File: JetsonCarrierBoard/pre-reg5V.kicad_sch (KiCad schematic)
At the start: 18 parts

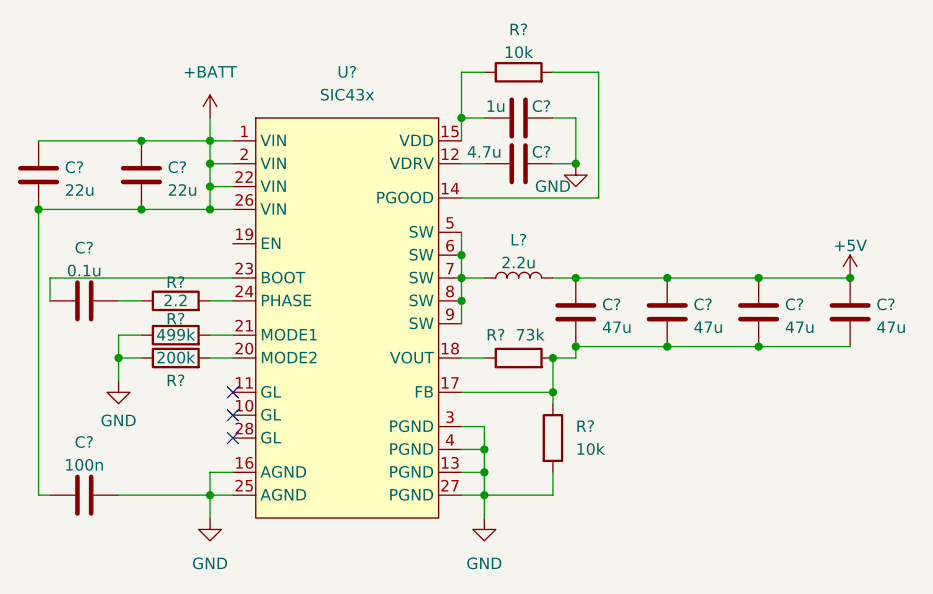
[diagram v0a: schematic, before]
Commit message: Part 2 of USB C wiring, renaming schematics
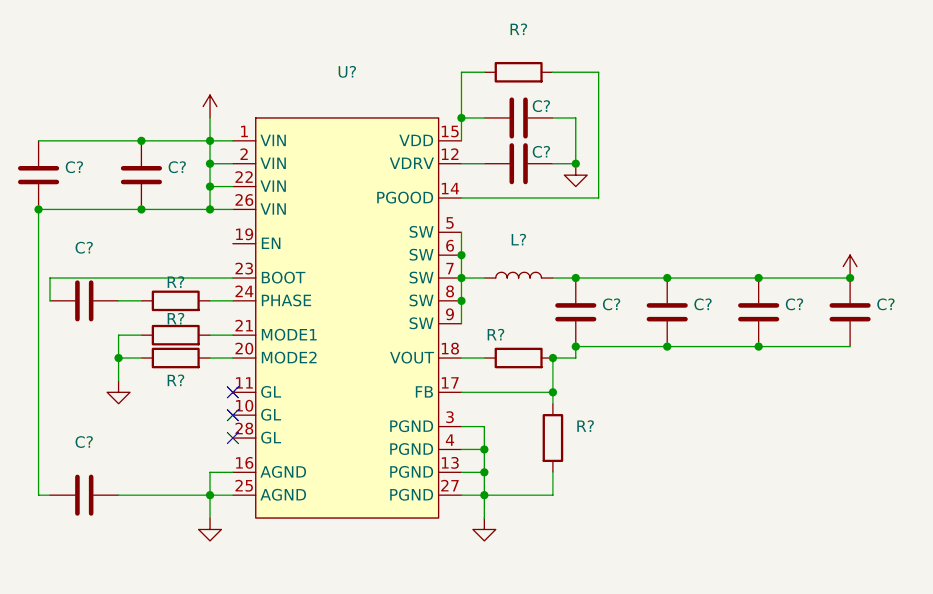
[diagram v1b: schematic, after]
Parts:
- C?: value 1u -> (none)
- C? (x4): value 47u -> (none)
- C?: value 4.7u -> (none)
- C?: value 0.1u -> (none)
- C? (x2): value 22u -> (none)
- C?: value 100n -> (none)
- L?: value 2.2u -> (none)
- R?: value 2.2 -> (none)
- R? (x2): value 10k -> (none)
- R?: value 200k -> (none)
- R?: value 73k -> (none)
- R?: value 499k -> (none)
- U?: value SIC43x -> (none)
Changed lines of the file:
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@@
     (in_bom yes) (on_board yes) (fields_autoplaced)
     (property "Reference" "U?" (id 0) (at 146.05 73.66 0))
-    (property "Value" "SIC43x" (id 1) (at 146.05 76.2 0))
+    (property "Value" "" (id 1) (at 146.05 76.2 0))
     (property "Footprint" "" (id 2) (at 151.13 80.01 0)
       (effects (font (size 1.27 1.27)) hide)
@@
     (in_bom yes) (on_board yes)
     (property "Reference" "C?" (id 0) (at 167.64 77.47 90))
-    (property "Value" "1u" (id 1) (at 162.56 77.47 90))
+    (property "Value" "" (id 1) (at 162.56 77.47 90))
     (property "Footprint" "" (id 2) (at 168.91 77.7748 0)
       (effects (font (size 1.27 1.27)) hide)
@@
       (effects (font (size 1.27 1.27)) (justify left))
     )
-    (property "Value" "47u" (id 1) (at 204.851 102.0322 0)
+    (property "Value" "" (id 1) (at 204.851 102.0322 0)
       (effects (font (size 1.27 1.27)) (justify left))
     )
@@
     (in_bom yes) (on_board yes)
     (property "Reference" "C?" (id 0) (at 167.64 82.55 90))
-    (property "Value" "4.7u" (id 1) (at 161.29 82.55 90))
+    (property "Value" "" (id 1) (at 161.29 82.55 90))
     (property "Footprint" "" (id 2) (at 168.91 82.8548 0)
       (effects (font (size 1.27 1.27)) hide)
@@
       (effects (font (size 1.27 1.27)) (justify left))
     )
-    (property "Value" "47u" (id 1) (at 184.531 102.0322 0)
+    (property "Value" "" (id 1) (at 184.531 102.0322 0)
       (effects (font (size 1.27 1.27)) (justify left))
     )
@@
       (effects (font (size 1.27 1.27)) (justify left))
     )
-    (property "Value" "47u" (id 1) (at 194.691 102.0322 0)
+    (property "Value" "" (id 1) (at 194.691 102.0322 0)
       (effects (font (size 1.27 1.27)) (justify left))
     )
@@
     (in_bom yes) (on_board yes)
     (property "Reference" "R?" (id 0) (at 127 97.028 90))
-    (property "Value" "2.2" (id 1) (at 127 99.06 90))
+    (property "Value" "" (id 1) (at 127 99.06 90))
     (property "Footprint" "" (id 2) (at 127 100.838 90)
       (effects (font (size 1.27 1.27)) hide)
@@
       (effects (font (size 1.27 1.27)) hide)
     )
-    (property "Value" "GND" (id 1) (at 130.81 128.27 0))
+    (property "Value" "" (id 1) (at 130.81 128.27 0))
     (property "Footprint" "" (id 2) (at 130.81 123.19 0)
       (effects (font (size 1.27 1.27)) hide)
@@
     (in_bom yes) (on_board yes) (fields_autoplaced)
     (property "Reference" "L?" (id 0) (at 165.1 92.3122 90))
-    (property "Value" "2.2u" (id 1) (at 165.1 94.8491 90))
+    (property "Value" "" (id 1) (at 165.1 94.8491 90))
     (property "Footprint" "" (id 2) (at 165.1 96.52 0)
       (effects (font (size 1.27 1.27)) hide)
@@
     (in_bom yes) (on_board yes) (fields_autoplaced)
     (property "Reference" "R?" (id 0) (at 165.1 68.9442 90))
-    (property "Value" "10k" (id 1) (at 165.1 71.4811 90))
+    (property "Value" "" (id 1) (at 165.1 71.4811 90))
     (property "Footprint" "" (id 2) (at 165.1 75.438 90)
       (effects (font (size 1.27 1.27)) hide)
@@
     (in_bom yes) (on_board yes) (fields_autoplaced)
     (property "Reference" "C?" (id 0) (at 116.84 93.2012 90))
-    (property "Value" "0.1u" (id 1) (at 116.84 95.7381 90))
+    (property "Value" "" (id 1) (at 116.84 95.7381 90))
     (property "Footprint" "" (id 2) (at 120.65 98.0948 0)
       (effects (font (size 1.27 1.27)) hide)
@@
       (effects (font (size 1.27 1.27)) (justify left))
     )
-    (property "Value" "47u" (id 1) (at 174.371 102.0322 0)
+    (property "Value" "" (id 1) (at 174.371 102.0322 0)
       (effects (font (size 1.27 1.27)) (justify left))
     )
@@
       (effects (font (size 1.27 1.27)) hide)
     )
-    (property "Value" "+5V" (id 1) (at 201.93 92.9442 0))
+    (property "Value" "" (id 1) (at 201.93 92.9442 0))
     (property "Footprint" "" (id 2) (at 201.93 96.52 0)
       (effects (font (size 1.27 1.27)) hide)
@@
     (in_bom yes) (on_board yes)
     (property "Reference" "R?" (id 0) (at 127 107.95 90))
-    (property "Value" "200k" (id 1) (at 127 105.41 90))
+    (property "Value" "" (id 1) (at 127 105.41 90))
     (property "Footprint" "" (id 2) (at 127 107.188 90)
       (effects (font (size 1.27 1.27)) hide)
@@
     (in_bom yes) (on_board yes)
     (property "Reference" "R?" (id 0) (at 162.56 102.87 90))
-    (property "Value" "73k" (id 1) (at 166.37 102.87 90))
+    (property "Value" "" (id 1) (at 166.37 102.87 90))
     (property "Footprint" "" (id 2) (at 165.1 107.188 90)
       (effects (font (size 1.27 1.27)) hide)
@@
       (effects (font (size 1.27 1.27)) hide)
     )
-    (property "Value" "+BATT" (id 1) (at 130.81 73.66 0))
+    (property "Value" "" (id 1) (at 130.81 73.66 0))
     (property "Footprint" "" (id 2) (at 130.81 78.74 0)
       (effects (font (size 1.27 1.27)) hide)
@@
       (effects (font (size 1.27 1.27)) hide)
     )
-    (property "Value" "GND" (id 1) (at 161.29 128.27 0))
+    (property "Value" "" (id 1) (at 161.29 128.27 0))
     (property "Footprint" "" (id 2) (at 161.29 123.19 0)
       (effects (font (size 1.27 1.27)) hide)
@@
       (effects (font (size 1.27 1.27)) (justify left))
     )
-    (property "Value" "10k" (id 1) (at 171.45 115.5699 0)
+    (property "Value" "" (id 1) (at 171.45 115.5699 0)
       (effects (font (size 1.27 1.27)) (justify left))
     )
@@
       (effects (font (size 1.27 1.27)) (justify left))
     )
-    (property "Value" "22u" (id 1) (at 126.111 86.7922 0)
+    (property "Value" "" (id 1) (at 126.111 86.7922 0)
       (effects (font (size 1.27 1.27)) (justify left))
     )
@@
       (effects (font (size 1.27 1.27)) (justify left))
     )
-    (property "Value" "22u" (id 1) (at 114.681 86.7922 0)
+    (property "Value" "" (id 1) (at 114.681 86.7922 0)
       (effects (font (size 1.27 1.27)) (justify left))
     )
@@
       (effects (font (size 1.27 1.27)) hide)
     )
-    (property "Value" "GND" (id 1) (at 168.91 86.36 0))
+    (property "Value" "" (id 1) (at 168.91 86.36 0))
     (property "Footprint" "" (id 2) (at 171.45 83.82 0)
       (effects (font (size 1.27 1.27)) hide)
@@
     (in_bom yes) (on_board yes) (fields_autoplaced)
     (property "Reference" "C?" (id 0) (at 116.84 114.7912 90))
-    (property "Value" "100n" (id 1) (at 116.84 117.3281 90))
+    (property "Value" "" (id 1) (at 116.84 117.3281 90))
     (property "Footprint" "" (id 2) (at 120.65 119.6848 0)
       (effects (font (size 1.27 1.27)) hide)
@@
       (effects (font (size 1.27 1.27)) hide)
     )
-    (property "Value" "GND" (id 1) (at 120.65 112.3934 0))
+    (property "Value" "" (id 1) (at 120.65 112.3934 0))
     (property "Footprint" "" (id 2) (at 120.65 107.95 0)
       (effects (font (size 1.27 1.27)) hide)
@@
     (in_bom yes) (on_board yes)
     (property "Reference" "R?" (id 0) (at 127 101.092 90))
-    (property "Value" "499k" (id 1) (at 127 102.87 90))
+    (property "Value" "" (id 1) (at 127 102.87 90))
     (property "Footprint" "" (id 2) (at 127 104.648 90)
       (effects (font (size 1.27 1.27)) hide)

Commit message: Finished USB-C w/ Alt mode and PD Wiring V1
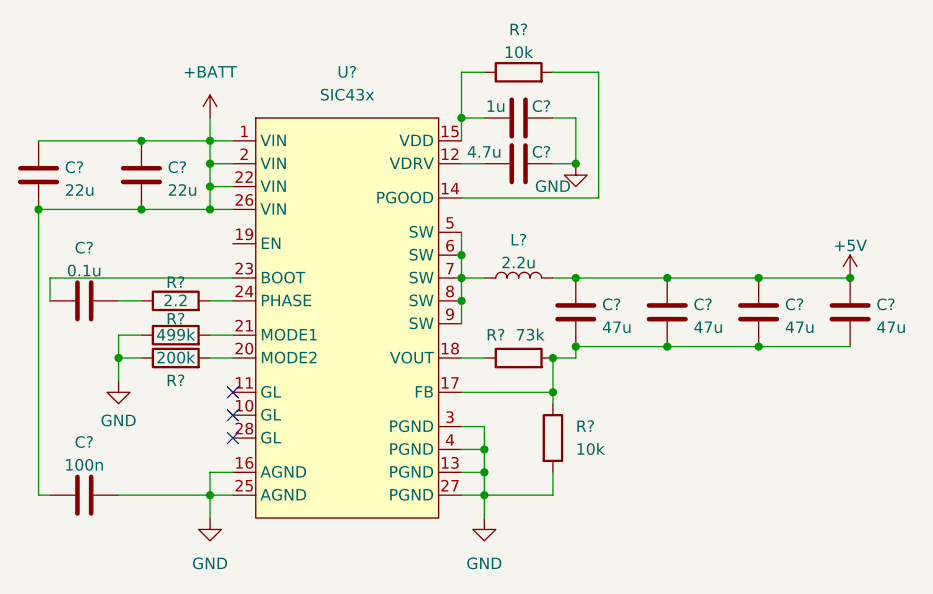
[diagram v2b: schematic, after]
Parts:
- C?: value (none) -> 1u
- C? (x4): value (none) -> 47u
- C?: value (none) -> 4.7u
- C?: value (none) -> 0.1u
- C? (x2): value (none) -> 22u
- C?: value (none) -> 100n
- L?: value (none) -> 2.2u
- R?: value (none) -> 2.2
- R? (x2): value (none) -> 10k
- R?: value (none) -> 200k
- R?: value (none) -> 73k
- R?: value (none) -> 499k
- U?: value (none) -> SIC43x
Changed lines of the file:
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@@
     (in_bom yes) (on_board yes) (fields_autoplaced)
     (property "Reference" "U?" (id 0) (at 146.05 73.66 0))
-    (property "Value" "" (id 1) (at 146.05 76.2 0))
+    (property "Value" "SIC43x" (id 1) (at 146.05 76.2 0))
     (property "Footprint" "" (id 2) (at 151.13 80.01 0)
       (effects (font (size 1.27 1.27)) hide)
@@
     (in_bom yes) (on_board yes)
     (property "Reference" "C?" (id 0) (at 167.64 77.47 90))
-    (property "Value" "" (id 1) (at 162.56 77.47 90))
+    (property "Value" "1u" (id 1) (at 162.56 77.47 90))
     (property "Footprint" "" (id 2) (at 168.91 77.7748 0)
       (effects (font (size 1.27 1.27)) hide)
@@
       (effects (font (size 1.27 1.27)) (justify left))
     )
-    (property "Value" "" (id 1) (at 204.851 102.0322 0)
+    (property "Value" "47u" (id 1) (at 204.851 102.0322 0)
       (effects (font (size 1.27 1.27)) (justify left))
     )
@@
     (in_bom yes) (on_board yes)
     (property "Reference" "C?" (id 0) (at 167.64 82.55 90))
-    (property "Value" "" (id 1) (at 161.29 82.55 90))
+    (property "Value" "4.7u" (id 1) (at 161.29 82.55 90))
     (property "Footprint" "" (id 2) (at 168.91 82.8548 0)
       (effects (font (size 1.27 1.27)) hide)
@@
       (effects (font (size 1.27 1.27)) (justify left))
     )
-    (property "Value" "" (id 1) (at 184.531 102.0322 0)
+    (property "Value" "47u" (id 1) (at 184.531 102.0322 0)
       (effects (font (size 1.27 1.27)) (justify left))
     )
@@
       (effects (font (size 1.27 1.27)) (justify left))
     )
-    (property "Value" "" (id 1) (at 194.691 102.0322 0)
+    (property "Value" "47u" (id 1) (at 194.691 102.0322 0)
       (effects (font (size 1.27 1.27)) (justify left))
     )
@@
     (in_bom yes) (on_board yes)
     (property "Reference" "R?" (id 0) (at 127 97.028 90))
-    (property "Value" "" (id 1) (at 127 99.06 90))
+    (property "Value" "2.2" (id 1) (at 127 99.06 90))
     (property "Footprint" "" (id 2) (at 127 100.838 90)
       (effects (font (size 1.27 1.27)) hide)
@@
       (effects (font (size 1.27 1.27)) hide)
     )
-    (property "Value" "" (id 1) (at 130.81 128.27 0))
+    (property "Value" "GND" (id 1) (at 130.81 128.27 0))
     (property "Footprint" "" (id 2) (at 130.81 123.19 0)
       (effects (font (size 1.27 1.27)) hide)
@@
     (in_bom yes) (on_board yes) (fields_autoplaced)
     (property "Reference" "L?" (id 0) (at 165.1 92.3122 90))
-    (property "Value" "" (id 1) (at 165.1 94.8491 90))
+    (property "Value" "2.2u" (id 1) (at 165.1 94.8491 90))
     (property "Footprint" "" (id 2) (at 165.1 96.52 0)
       (effects (font (size 1.27 1.27)) hide)
@@
     (in_bom yes) (on_board yes) (fields_autoplaced)
     (property "Reference" "R?" (id 0) (at 165.1 68.9442 90))
-    (property "Value" "" (id 1) (at 165.1 71.4811 90))
+    (property "Value" "10k" (id 1) (at 165.1 71.4811 90))
     (property "Footprint" "" (id 2) (at 165.1 75.438 90)
       (effects (font (size 1.27 1.27)) hide)
@@
     (in_bom yes) (on_board yes) (fields_autoplaced)
     (property "Reference" "C?" (id 0) (at 116.84 93.2012 90))
-    (property "Value" "" (id 1) (at 116.84 95.7381 90))
+    (property "Value" "0.1u" (id 1) (at 116.84 95.7381 90))
     (property "Footprint" "" (id 2) (at 120.65 98.0948 0)
       (effects (font (size 1.27 1.27)) hide)
@@
       (effects (font (size 1.27 1.27)) (justify left))
     )
-    (property "Value" "" (id 1) (at 174.371 102.0322 0)
+    (property "Value" "47u" (id 1) (at 174.371 102.0322 0)
       (effects (font (size 1.27 1.27)) (justify left))
     )
@@
       (effects (font (size 1.27 1.27)) hide)
     )
-    (property "Value" "" (id 1) (at 201.93 92.9442 0))
+    (property "Value" "+5V" (id 1) (at 201.93 92.9442 0))
     (property "Footprint" "" (id 2) (at 201.93 96.52 0)
       (effects (font (size 1.27 1.27)) hide)
@@
     (in_bom yes) (on_board yes)
     (property "Reference" "R?" (id 0) (at 127 107.95 90))
-    (property "Value" "" (id 1) (at 127 105.41 90))
+    (property "Value" "200k" (id 1) (at 127 105.41 90))
     (property "Footprint" "" (id 2) (at 127 107.188 90)
       (effects (font (size 1.27 1.27)) hide)
@@
     (in_bom yes) (on_board yes)
     (property "Reference" "R?" (id 0) (at 162.56 102.87 90))
-    (property "Value" "" (id 1) (at 166.37 102.87 90))
+    (property "Value" "73k" (id 1) (at 166.37 102.87 90))
     (property "Footprint" "" (id 2) (at 165.1 107.188 90)
       (effects (font (size 1.27 1.27)) hide)
@@
       (effects (font (size 1.27 1.27)) hide)
     )
-    (property "Value" "" (id 1) (at 130.81 73.66 0))
+    (property "Value" "+BATT" (id 1) (at 130.81 73.66 0))
     (property "Footprint" "" (id 2) (at 130.81 78.74 0)
       (effects (font (size 1.27 1.27)) hide)
@@
       (effects (font (size 1.27 1.27)) hide)
     )
-    (property "Value" "" (id 1) (at 161.29 128.27 0))
+    (property "Value" "GND" (id 1) (at 161.29 128.27 0))
     (property "Footprint" "" (id 2) (at 161.29 123.19 0)
       (effects (font (size 1.27 1.27)) hide)
@@
       (effects (font (size 1.27 1.27)) (justify left))
     )
-    (property "Value" "" (id 1) (at 171.45 115.5699 0)
+    (property "Value" "10k" (id 1) (at 171.45 115.5699 0)
       (effects (font (size 1.27 1.27)) (justify left))
     )
@@
       (effects (font (size 1.27 1.27)) (justify left))
     )
-    (property "Value" "" (id 1) (at 126.111 86.7922 0)
+    (property "Value" "22u" (id 1) (at 126.111 86.7922 0)
       (effects (font (size 1.27 1.27)) (justify left))
     )
@@
       (effects (font (size 1.27 1.27)) (justify left))
     )
-    (property "Value" "" (id 1) (at 114.681 86.7922 0)
+    (property "Value" "22u" (id 1) (at 114.681 86.7922 0)
       (effects (font (size 1.27 1.27)) (justify left))
     )
@@
       (effects (font (size 1.27 1.27)) hide)
     )
-    (property "Value" "" (id 1) (at 168.91 86.36 0))
+    (property "Value" "GND" (id 1) (at 168.91 86.36 0))
     (property "Footprint" "" (id 2) (at 171.45 83.82 0)
       (effects (font (size 1.27 1.27)) hide)
@@
     (in_bom yes) (on_board yes) (fields_autoplaced)
     (property "Reference" "C?" (id 0) (at 116.84 114.7912 90))
-    (property "Value" "" (id 1) (at 116.84 117.3281 90))
+    (property "Value" "100n" (id 1) (at 116.84 117.3281 90))
     (property "Footprint" "" (id 2) (at 120.65 119.6848 0)
       (effects (font (size 1.27 1.27)) hide)
@@
       (effects (font (size 1.27 1.27)) hide)
     )
-    (property "Value" "" (id 1) (at 120.65 112.3934 0))
+    (property "Value" "GND" (id 1) (at 120.65 112.3934 0))
     (property "Footprint" "" (id 2) (at 120.65 107.95 0)
       (effects (font (size 1.27 1.27)) hide)
@@
     (in_bom yes) (on_board yes)
     (property "Reference" "R?" (id 0) (at 127 101.092 90))
-    (property "Value" "" (id 1) (at 127 102.87 90))
+    (property "Value" "499k" (id 1) (at 127 102.87 90))
     (property "Footprint" "" (id 2) (at 127 104.648 90)
       (effects (font (size 1.27 1.27)) hide)
